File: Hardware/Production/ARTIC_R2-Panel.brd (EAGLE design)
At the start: 113 x 116.3 mm, 1142 parts, among them J1 U.FL, J10 THING_PLUS, J11 U.FL, J12 Flash Programming, J13 THING_PLUS, J14 U.FL, J15 Flash Programming, J16 THING_PLUS, J17 U.FL, J18 Flash Programming, J19 THING_PLUS, J2 THING_PLUS, J20 U.FL, J21 Flash Programming, J22 THING_PLUS, J23 U.FL, J24 Flash Programming, J3 THING_PLUS, J4 U.FL, J5 Flash Programming, J6 Flash Programming, J7 THING_PLUS, J8 U.FL, J9 Flash Programming, K1 TLP3475R, K2 TLP3475R, K3 TLP3475R, K4 TLP3475R, K5 TLP3475R, K6 TLP3475R, K7 TLP3475R, K8 TLP3475R, Q1 3.1A/30V/105mΩ, Q2 3.1A/30V/105mΩ, Q3 3.1A/30V/105mΩ, Q4 3.1A/30V/105mΩ, Q5 3.1A/30V/105mΩ, Q6 3.1A/30V/105mΩ, Q7 3.1A/30V/105mΩ, Q8 3.1A/30V/105mΩ, U1 2Mbit SPI Flash, U10 RFPA0133, U11 AS179-92LF, U12 1.8V/100mA, U13 2Mbit SPI Flash, U14 3.3V, U15 3.3V, U16 3.0V, U17 ARTIC_R2, U18 RFPA0133, U19 AS179-92LF, U2 1.8V/100mA, U20 1.8V/100mA, U21 2Mbit SPI Flash, U22 3.3V, U23 3.3V, U24 3.0V, U25 ARTIC_R2, U26 RFPA0133, U27 AS179-92LF, U28 1.8V/100mA, U29 2Mbit SPI Flash, U3 ARTIC_R2, U30 3.3V, U31 3.3V, U32 3.0V, U33 ARTIC_R2, U34 RFPA0133, U35 AS179-92LF, U36 1.8V/100mA, U37 2Mbit SPI Flash, U38 3.3V, U39 3.3V, U4 RFPA0133, U40 3.0V, U41 ARTIC_R2, U42 RFPA0133, U43 AS179-92LF, U44 1.8V/100mA, U45 2Mbit SPI Flash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

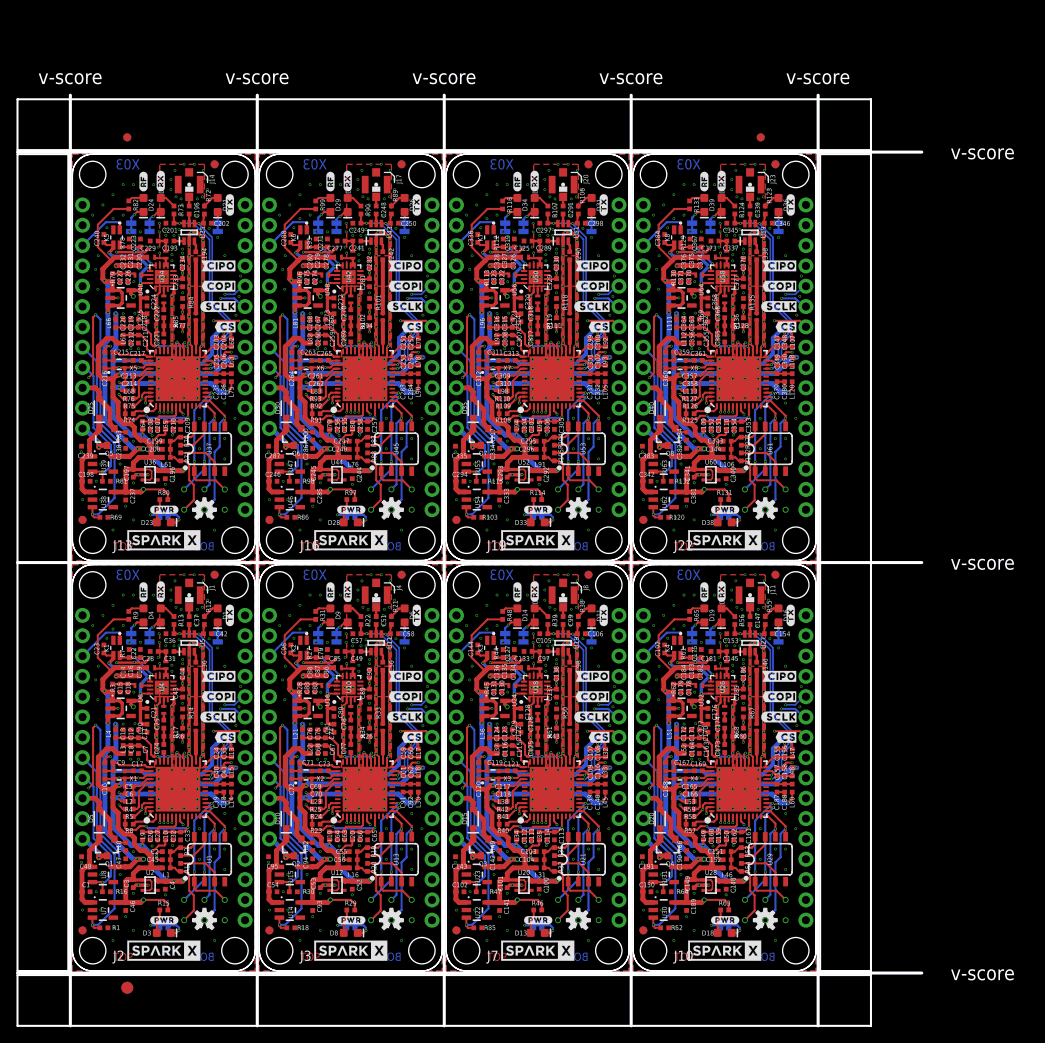
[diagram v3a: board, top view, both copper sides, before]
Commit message: Final tweaks for X03. Changed 8dB to G8. Increased annular ring to 3.5mil.
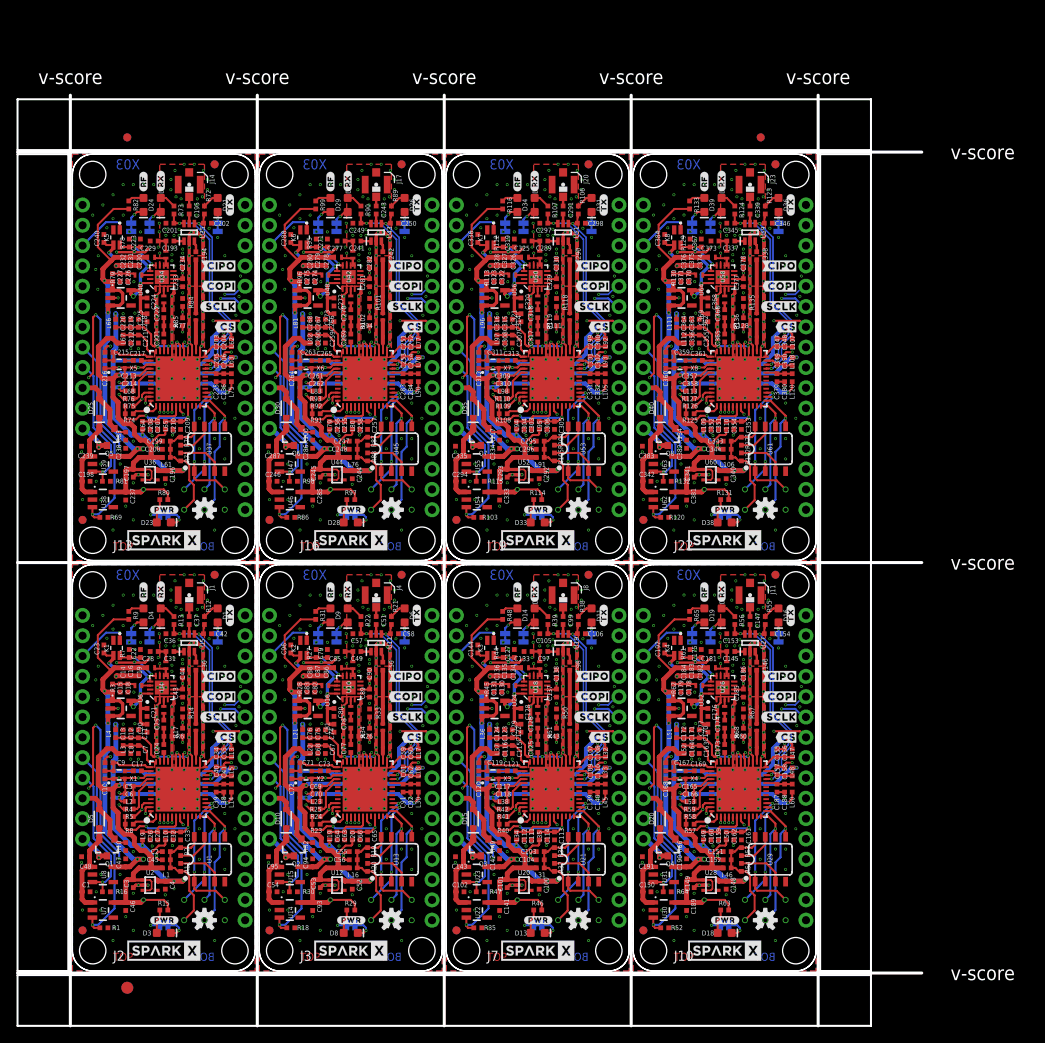
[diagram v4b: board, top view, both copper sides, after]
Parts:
- U$108, U$135, U$162, U$189, U$216, U$54, U$6, U$81: device output:#8DB#0 -> output:#G8#0
- moved U$108 0.38 mm to (73.9, 39.4)
- moved U$162 0.38 mm to (27.2, 90.7)
- moved U$189 0.38 mm to (50.5, 90.7)
- moved U$216 0.38 mm to (73.9, 90.7)
- moved U$54 0.38 mm to (27.2, 39.4)
- moved U$81 0.38 mm to (50.5, 39.4)
- moved U$135 0.38 mm to (3.81, 90.7)
- moved U$6 0.38 mm to (3.81, 39.4)
- moved C109 0.13 mm to (64.7, 25.0)
- moved C157 0.13 mm to (88.1, 25.0)
- moved C40 0.13 mm to (18.0, 25.0)
- moved C61 0.13 mm to (41.3, 25.0)
- moved C205 0.13 mm to (18.0, 76.3)
- moved C253 0.13 mm to (41.3, 76.3)
- moved C301 0.13 mm to (64.7, 76.3)
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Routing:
- net VREF8: track 19.9 -> 21.9 mm
- net VREF6: track 19.9 -> 21.9 mm
- net VREF2: track 19.9 -> 21.9 mm
- net VREF7: track 19.9 -> 21.9 mm
- net VREF4: track 19.9 -> 21.9 mm
- net VREF3: track 19.9 -> 21.9 mm
- net VREF1: track 19.9 -> 21.9 mm
- net VREF5: track 19.9 -> 21.9 mm
